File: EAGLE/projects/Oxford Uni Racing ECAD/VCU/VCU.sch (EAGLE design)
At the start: 77 parts, among them IC2 LM2901D, IC3 4081D, J1 Connector A, J2 Connector C, D, ii, J3 MC_LEFT, J4 MC_RIGHT, J5 Connector 3, J6 LEFT_COOLING_SENSOR, J8 RIGHT_COOLING_SENSOR, K1 RT444012, T2 BT169, U1 REF3040AIDBZT, U3 TLV4170IDR, X1 Connector i, X2 D-SUB9-H2M09ST

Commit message: fixed ass connections
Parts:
- U1: value REF3040AIDBZT -> REF3020AIDBZT
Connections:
- new net ASS_INTERNAL: K12.P, K13.P, RELAY12.P, RELAY13.P
- net ASS1: no longer K12.S, K13.S
- net ASS2: now also K12.S, K13.S; no longer K12.P, K13.P, RELAY12.P, RELAY13.P
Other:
- moved on the sheet: K1
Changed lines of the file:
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@@
 <part name="SUPPLY25" library="SparkFun-PowerSymbols" library_urn="urn:adsk.eagle:library:530" deviceset="5V" device=""/>
 <part name="GND8" library="SparkFun-PowerSymbols" library_urn="urn:adsk.eagle:library:530" deviceset="GND" device=""/>
-<part name="U1" library="SparkFun-DiscreteSemi" library_urn="urn:adsk.eagle:library:514" deviceset="LM4051" device="" package3d_urn="urn:adsk.eagle:package:38446/1" value="REF3040AIDBZT"/>
+<part name="U1" library="SparkFun-DiscreteSemi" library_urn="urn:adsk.eagle:library:514" deviceset="LM4051" device="" package3d_urn="urn:adsk.eagle:package:38446/1" value="REF3020AIDBZT"/>
 <part name="SUPPLY34" library="SparkFun-PowerSymbols" library_urn="urn:adsk.eagle:library:530" deviceset="5V" device=""/>
 <part name="GND26" library="SparkFun-PowerSymbols" library_urn="urn:adsk.eagle:library:530" deviceset="GND" device=""/>
@@
 <attribute name="PART" x="361.95" y="142.24" size="1.778" layer="95"/>
 </instance>
-<instance part="K1" gate="2" x="378.46" y="137.16" smashed="yes">
-<attribute name="PART" x="375.92" y="134.62" size="1.778" layer="95" rot="R90"/>
+<instance part="K1" gate="2" x="378.46" y="137.16" smashed="yes" rot="R180">
+<attribute name="PART" x="381" y="139.7" size="1.778" layer="95" rot="R270"/>
 </instance>
-<instance part="K1" gate="3" x="386.08" y="137.16" smashed="yes">
-<attribute name="PART" x="383.54" y="134.62" size="1.778" layer="95" rot="R90"/>
+<instance part="K1" gate="3" x="386.08" y="137.16" smashed="yes" rot="R180">
+<attribute name="PART" x="388.62" y="139.7" size="1.778" layer="95" rot="R270"/>
 </instance>
 <instance part="R1" gate="G$1" x="340.36" y="114.3" smashed="yes">
@@
 <net name="ASS1" class="0">
 <segment>
-<label x="386.08" y="149.86" size="1.778" layer="95" rot="R90"/>
-<pinref part="K1" gate="3" pin="S"/>
-<wire x1="386.08" y1="147.32" x2="386.08" y2="144.78" width="0.1524" layer="91"/>
-<wire x1="386.08" y1="144.78" x2="386.08" y2="142.24" width="0.1524" layer="91"/>
-<wire x1="386.08" y1="144.78" x2="378.46" y2="144.78" width="0.1524" layer="91"/>
-<junction x="386.08" y="144.78"/>
-<pinref part="K1" gate="2" pin="S"/>
-<wire x1="378.46" y1="144.78" x2="378.46" y2="142.24" width="0.1524" layer="91"/>
-</segment>
-<segment>
 <label x="10.16" y="76.2" size="1.778" layer="95"/>
 <wire x1="10.16" y1="76.2" x2="0" y2="76.2" width="0.1524" layer="91"/>
@@
 <segment>
 <label x="386.08" y="119.38" size="1.778" layer="95" rot="R90"/>
-<pinref part="K1" gate="3" pin="P"/>
 <wire x1="386.08" y1="127" x2="386.08" y2="129.54" width="0.1524" layer="91"/>
-<wire x1="386.08" y1="129.54" x2="386.08" y2="132.08" width="0.1524" layer="91"/>
 <wire x1="386.08" y1="129.54" x2="378.46" y2="129.54" width="0.1524" layer="91"/>
+<pinref part="K1" gate="2" pin="S"/>
+<wire x1="378.46" y1="132.08" x2="378.46" y2="129.54" width="0.1524" layer="91"/>
+<pinref part="K1" gate="3" pin="S"/>
+<wire x1="386.08" y1="132.08" x2="386.08" y2="129.54" width="0.1524" layer="91"/>
 <junction x="386.08" y="129.54"/>
-<pinref part="K1" gate="2" pin="P"/>
-<wire x1="378.46" y1="129.54" x2="378.46" y2="132.08" width="0.1524" layer="91"/>
 </segment>
 <segment>
@@
 </segment>
 </net>
+<net name="ASS_INTERNAL" class="0">
+<segment>
+<wire x1="386.08" y1="144.78" x2="386.08" y2="149.86" width="0.1524" layer="91"/>
+<wire x1="378.46" y1="144.78" x2="386.08" y2="144.78" width="0.1524" layer="91"/>
+<label x="386.08" y="149.86" size="1.778" layer="95"/>
+<pinref part="K1" gate="3" pin="P"/>
+<wire x1="386.08" y1="142.24" x2="386.08" y2="144.78" width="0.1524" layer="91"/>
+<junction x="386.08" y="144.78"/>
+<pinref part="K1" gate="2" pin="P"/>
+<wire x1="378.46" y1="144.78" x2="378.46" y2="142.24" width="0.1524" layer="91"/>
+</segment>
+</net>
 </nets>
 </sheet>
@@
 </segment>
 </net>
-<net name="ASS2" class="0">
-<segment>
-<pinref part="RELAY1" gate="2" pin="P"/>
-<wire x1="243.84" y1="66.04" x2="243.84" y2="71.12" width="0.1524" layer="91"/>
-<label x="243.84" y="58.42" size="1.778" layer="95" rot="R90"/>
-<pinref part="RELAY1" gate="3" pin="P"/>
-<wire x1="243.84" y1="71.12" x2="243.84" y2="73.66" width="0.1524" layer="91"/>
-<wire x1="254" y1="73.66" x2="254" y2="71.12" width="0.1524" layer="91"/>
-<wire x1="254" y1="71.12" x2="243.84" y2="71.12" width="0.1524" layer="91"/>
-<junction x="243.84" y="71.12"/>
-</segment>
-</net>
 <net name="CURR_S_SIG" class="0">
 <segment>
@@
 </segment>
 </net>
+<net name="ASS_INTERNAL" class="0">
+<segment>
+<pinref part="RELAY1" gate="2" pin="P"/>
+<wire x1="243.84" y1="73.66" x2="243.84" y2="71.12" width="0.1524" layer="91"/>
+<pinref part="RELAY1" gate="3" pin="P"/>
+<wire x1="243.84" y1="71.12" x2="243.84" y2="66.04" width="0.1524" layer="91"/>
+<wire x1="254" y1="73.66" x2="254" y2="71.12" width="0.1524" layer="91"/>
+<wire x1="254" y1="71.12" x2="243.84" y2="71.12" width="0.1524" layer="91"/>
+<junction x="243.84" y="71.12"/>
+<label x="243.84" y="63.5" size="1.778" layer="95" rot="R270"/>
+</segment>
+</net>

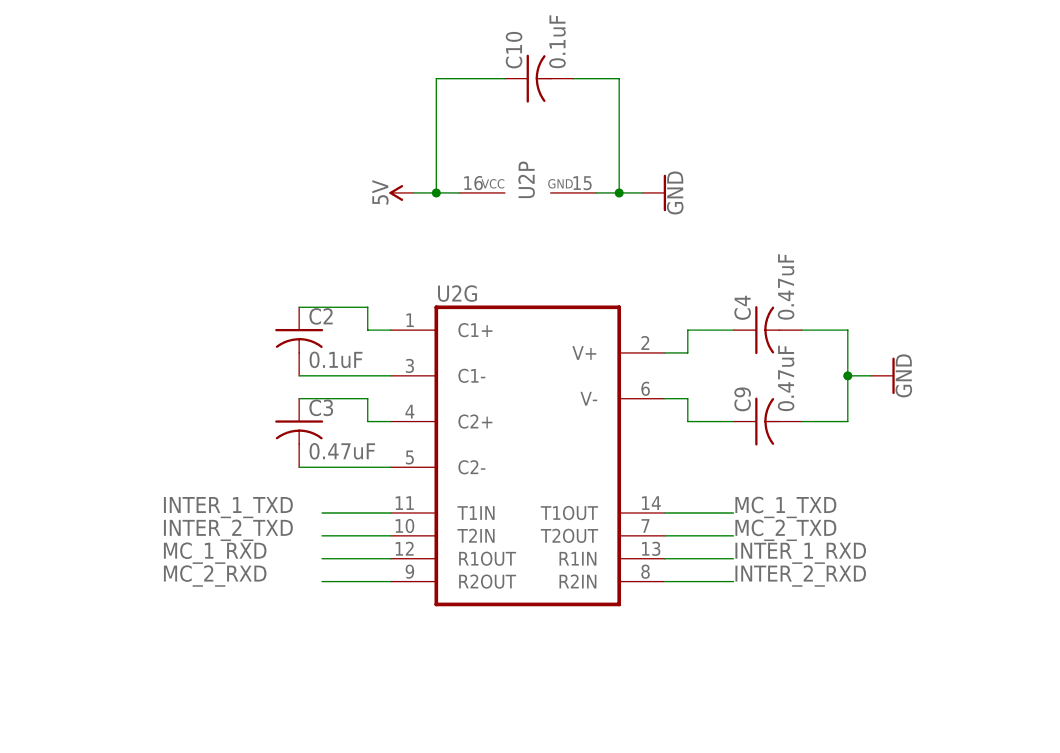
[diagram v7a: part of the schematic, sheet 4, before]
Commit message: fixed RS3232 wiring
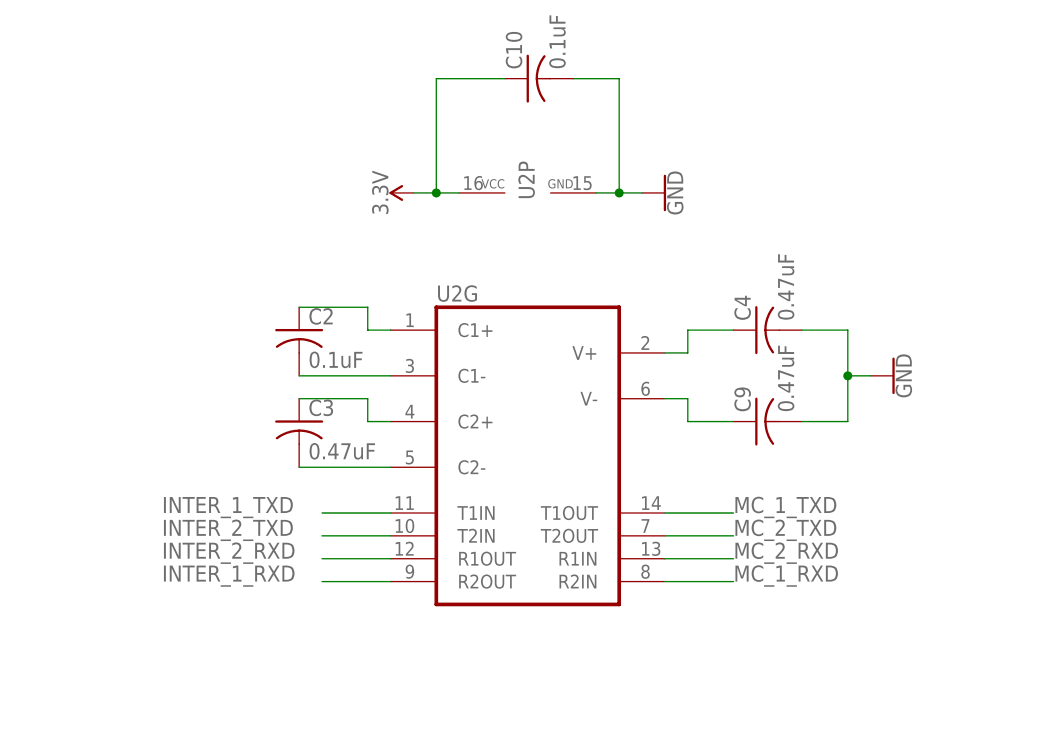
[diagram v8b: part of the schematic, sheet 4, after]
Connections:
- net 3.3V: now also C10.1, U2P.VCC
- net 5V: no longer C10.1, U2P.VCC
- net INTER_1_RXD: now also U2G.R2OUT; no longer U2G.R1IN
- net INTER_2_RXD: now also U2G.R1OUT; no longer U2G.R2IN
- net MC_1_RXD: now also U2G.R2IN; no longer U2G.R1OUT
- net MC_2_RXD: now also U2G.R1IN; no longer U2G.R2OUT
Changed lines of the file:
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@@
 <part name="U2" library="m-pad-2.1" deviceset="MAX3232" device="S"/>
 <part name="GND29" library="SparkFun-PowerSymbols" library_urn="urn:adsk.eagle:library:530" deviceset="GND" device=""/>
-<part name="SUPPLY20" library="SparkFun-PowerSymbols" library_urn="urn:adsk.eagle:library:530" deviceset="5V" device=""/>
 <part name="C2" library="adafruit" library_urn="urn:adsk.eagle:library:420" deviceset="C-US" device="025-024X044" package3d_urn="urn:adsk.eagle:package:6240324/1" value="0.1uF"/>
 <part name="C3" library="adafruit" library_urn="urn:adsk.eagle:library:420" deviceset="C-US" device="025-024X044" package3d_urn="urn:adsk.eagle:package:6240324/1" value="0.47uF"/>
@@
 <part name="C12" library="adafruit" library_urn="urn:adsk.eagle:library:420" deviceset="C-US" device="050-024X044" package3d_urn="urn:adsk.eagle:package:6240356/1" value="0.1uF"/>
 <part name="C13" library="adafruit" library_urn="urn:adsk.eagle:library:420" deviceset="C-US" device="050-024X044" package3d_urn="urn:adsk.eagle:package:6240356/1" value="0.47uF"/>
+<part name="SUPPLY20" library="SparkFun-PowerSymbols" library_urn="urn:adsk.eagle:library:530" deviceset="3.3V" device=""/>
 </parts>
 <sheets>
@@
 <attribute name="VALUE" x="226.314" y="195.58" size="1.778" layer="96" rot="R90" align="top-center"/>
 </instance>
-<instance part="SUPPLY20" gate="G$1" x="198.12" y="195.58" smashed="yes" rot="R90">
-<attribute name="VALUE" x="195.326" y="195.58" size="1.778" layer="96" rot="R90" align="bottom-center"/>
-</instance>
 <instance part="C2" gate="G$1" x="185.42" y="180.34" smashed="yes">
 <attribute name="NAME" x="186.436" y="180.975" size="1.778" layer="95"/>
@@
 <attribute name="NAME" x="308.356" y="117.475" size="1.778" layer="95"/>
 <attribute name="VALUE" x="308.356" y="112.649" size="1.778" layer="96"/>
+</instance>
+<instance part="SUPPLY20" gate="G$1" x="198.12" y="195.58" smashed="yes" rot="R90">
+<attribute name="VALUE" x="195.326" y="195.58" size="1.778" layer="96" rot="R90" align="bottom-center"/>
 </instance>
 </instances>
@@
 </segment>
 <segment>
-<pinref part="U2" gate="P" pin="VCC"/>
-<pinref part="SUPPLY20" gate="G$1" pin="5V"/>
-<wire x1="203.2" y1="195.58" x2="200.66" y2="195.58" width="0.1524" layer="91"/>
-<pinref part="C10" gate="G$1" pin="1"/>
-<wire x1="200.66" y1="195.58" x2="198.12" y2="195.58" width="0.1524" layer="91"/>
-<wire x1="200.66" y1="195.58" x2="200.66" y2="208.28" width="0.1524" layer="91"/>
-<wire x1="200.66" y1="208.28" x2="208.28" y2="208.28" width="0.1524" layer="91"/>
-<junction x="200.66" y="195.58"/>
-</segment>
-<segment>
 <label x="10.16" y="93.98" size="1.778" layer="95"/>
 <pinref part="SUPPLY11" gate="G$1" pin="5V"/>
@@
 <pinref part="SUPPLY12" gate="G$1" pin="3.3V"/>
 <wire x1="33.02" y1="91.44" x2="0" y2="91.44" width="0.1524" layer="91"/>
+</segment>
+<segment>
+<pinref part="U2" gate="P" pin="VCC"/>
+<wire x1="203.2" y1="195.58" x2="200.66" y2="195.58" width="0.1524" layer="91"/>
+<pinref part="C10" gate="G$1" pin="1"/>
+<wire x1="200.66" y1="195.58" x2="198.12" y2="195.58" width="0.1524" layer="91"/>
+<wire x1="200.66" y1="195.58" x2="200.66" y2="208.28" width="0.1524" layer="91"/>
+<wire x1="200.66" y1="208.28" x2="208.28" y2="208.28" width="0.1524" layer="91"/>
+<junction x="200.66" y="195.58"/>
+<pinref part="SUPPLY20" gate="G$1" pin="3.3V"/>
 </segment>
 </net>
@@
 <net name="MC_1_RXD" class="0">
 <segment>
-<pinref part="U2" gate="G" pin="R1OUT"/>
-<wire x1="195.58" y1="154.94" x2="187.96" y2="154.94" width="0.1524" layer="91"/>
-<label x="170.18" y="154.94" size="1.778" layer="95"/>
-</segment>
-<segment>
 <label x="10.16" y="63.5" size="1.778" layer="95"/>
 <wire x1="10.16" y1="63.5" x2="0" y2="63.5" width="0.1524" layer="91"/>
+</segment>
+<segment>
+<wire x1="233.68" y1="152.4" x2="226.06" y2="152.4" width="0.1524" layer="91"/>
+<label x="233.68" y="152.4" size="1.778" layer="95"/>
+<pinref part="U2" gate="G" pin="R2IN"/>
 </segment>
 </net>
@@
 <net name="MC_2_RXD" class="0">
 <segment>
-<pinref part="U2" gate="G" pin="R2OUT"/>
-<wire x1="195.58" y1="152.4" x2="187.96" y2="152.4" width="0.1524" layer="91"/>
-<label x="170.18" y="152.4" size="1.778" layer="95"/>
-</segment>
-<segment>
 <label x="10.16" y="43.18" size="1.778" layer="95"/>
 <wire x1="10.16" y1="43.18" x2="0" y2="43.18" width="0.1524" layer="91"/>
+</segment>
+<segment>
+<wire x1="233.68" y1="154.94" x2="226.06" y2="154.94" width="0.1524" layer="91"/>
+<label x="233.68" y="154.94" size="1.778" layer="95"/>
+<pinref part="U2" gate="G" pin="R1IN"/>
 </segment>
 </net>
@@
 </segment>
 <segment>
-<pinref part="U2" gate="G" pin="R2IN"/>
-<wire x1="226.06" y1="152.4" x2="233.68" y2="152.4" width="0.1524" layer="91"/>
-<label x="233.68" y="152.4" size="1.778" layer="95"/>
+<wire x1="195.58" y1="154.94" x2="187.96" y2="154.94" width="0.1524" layer="91"/>
+<label x="170.18" y="154.94" size="1.778" layer="95"/>
+<pinref part="U2" gate="G" pin="R1OUT"/>
 </segment>
 </net>
@@
 </segment>
 <segment>
-<pinref part="U2" gate="G" pin="R1IN"/>
-<wire x1="226.06" y1="154.94" x2="233.68" y2="154.94" width="0.1524" layer="91"/>
-<label x="233.68" y="154.94" size="1.778" layer="95"/>
-</segment>
-</net>
+<wire x1="195.58" y1="152.4" x2="187.96" y2="152.4" width="0.1524" layer="91"/>
+<label x="170.18" y="152.4" size="1.778" layer="95"/>
+<pinref part="U2" gate="G" pin="R2OUT"/>
+</segment>
+</net>
